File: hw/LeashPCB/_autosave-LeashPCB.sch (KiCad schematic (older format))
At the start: 11 parts, among them J1 Conn_02x03_Odd_Even, J2 1020-1, J3 1020-1, J4 1020-1, J5 1020-1, SW1 SW_Push, U1 CC1352R

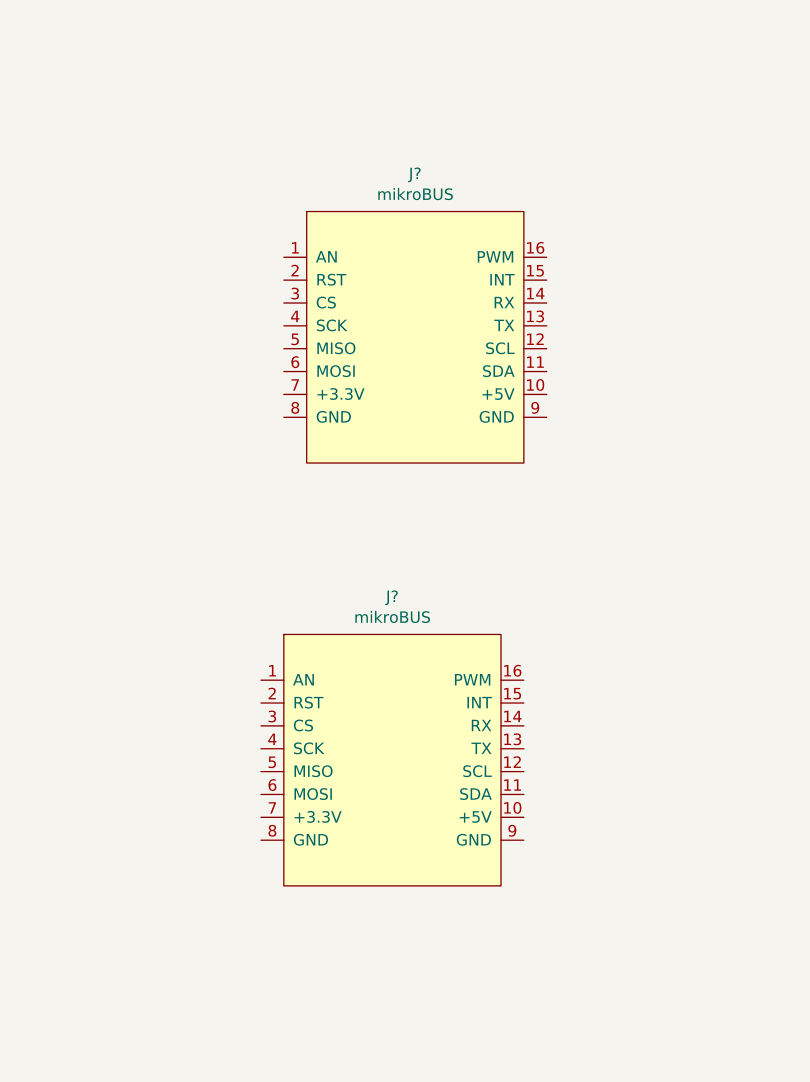
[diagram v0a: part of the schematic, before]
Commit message: Added first pass try at the mechanicals/batteries using SMT components and AAAA batteries
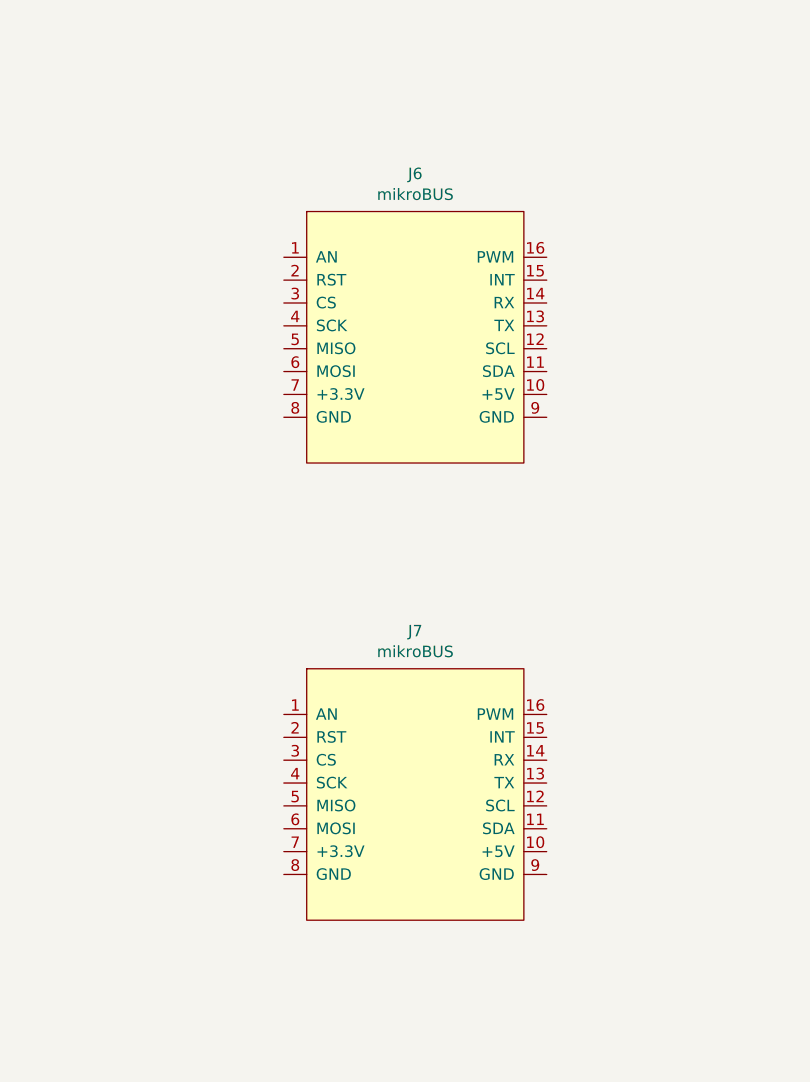
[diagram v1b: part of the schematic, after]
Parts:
- removed J?: mikroBUS, leash:mikroBUS, symbol LeashPCB:mikroBUS
- added J7: mikroBUS, leash:MikroBus-SMD, symbol LeashPCB:mikroBUS
- J6: renamed from J?; footprint leash:mikroBUS -> leash:MikroBus-SMD
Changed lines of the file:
@@
 $EndComp
 $Comp
-L LeashPCB:mikroBUS J?
+L LeashPCB:mikroBUS J6
 U 1 1 5D0322BE
 P 13700 4600
-F 0 "J?" H 13725 5315 50  0000 C CNN
+F 0 "J6" H 13725 5315 50  0000 C CNN
 F 1 "mikroBUS" H 13725 5224 50  0000 C CNN
-F 2 "leash:mikroBUS" H 13500 4800 50  0001 C CNN
+F 2 "leash:MikroBus-SMD" H 13500 4800 50  0001 C CNN
 F 3 "" H 13500 4800 50  0001 C CNN
 	1    13700 4600
@@
 $EndComp
 $Comp
-L LeashPCB:mikroBUS J?
-U 1 1 5D0329EE
-P 13600 6450
-F 0 "J?" H 13625 7165 50  0000 C CNN
-F 1 "mikroBUS" H 13625 7074 50  0000 C CNN
-F 2 "leash:mikroBUS" H 13400 6650 50  0001 C CNN
-F 3 "" H 13400 6650 50  0001 C CNN
-	1    13600 6450
+L LeashPCB:mikroBUS J7
+U 1 1 5D0335F5
+P 13700 6600
+F 0 "J7" H 13725 7315 50  0000 C CNN
+F 1 "mikroBUS" H 13725 7224 50  0000 C CNN
+F 2 "leash:MikroBus-SMD" H 13500 6800 50  0001 C CNN
+F 3 "" H 13500 6800 50  0001 C CNN
+	1    13700 6600
 	1    0    0    -1
 $EndComp
